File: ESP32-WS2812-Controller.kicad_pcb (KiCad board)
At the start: 2 copper layers, 60 x 50 mm, 29 parts, among them J1 USB_B_Micro, J2 Alternate_Power_Input, J3 Conn_02x03_Odd_Even, J4 Conn_01x03, Q1 Q_NPN_BEC, SW1 SW_Push, U1 AP2114HA-3.3, U2 ESP32-WROOM

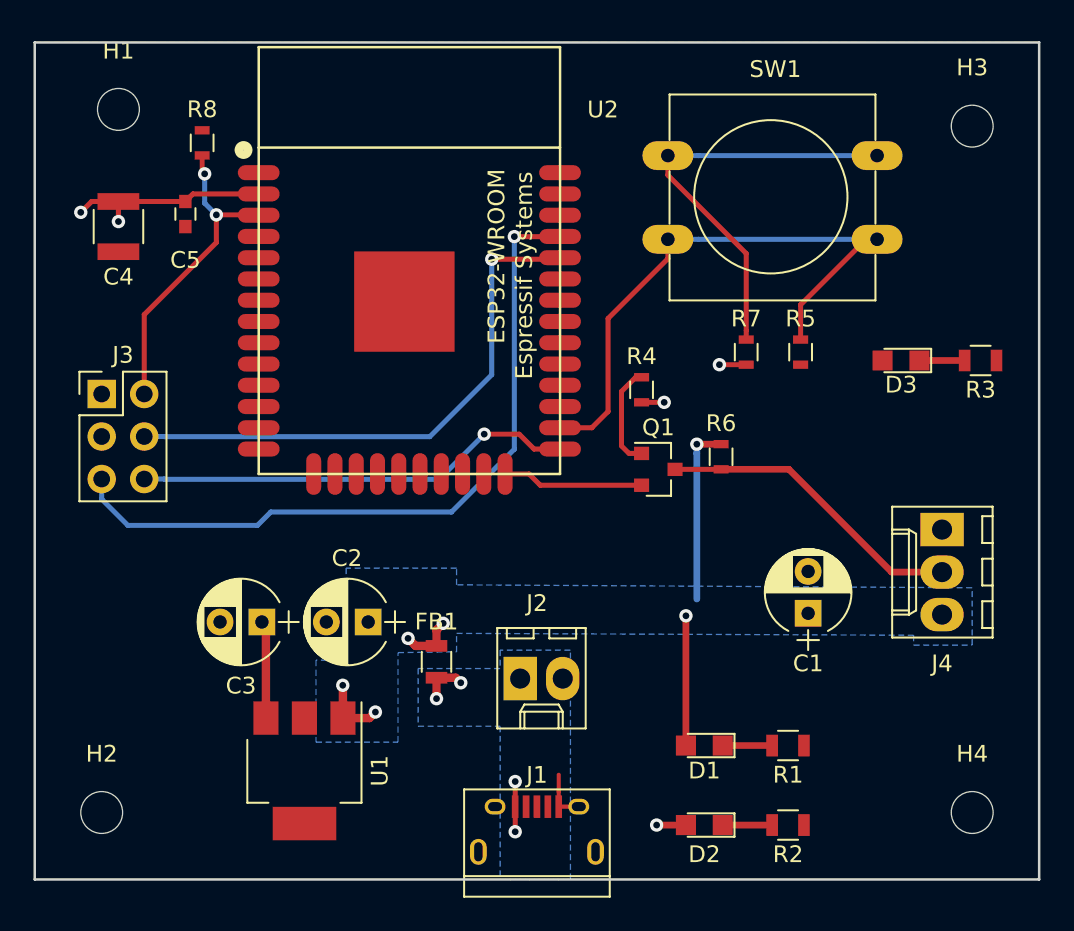
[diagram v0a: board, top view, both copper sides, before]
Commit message: Added ADC & power breakout for microphone board
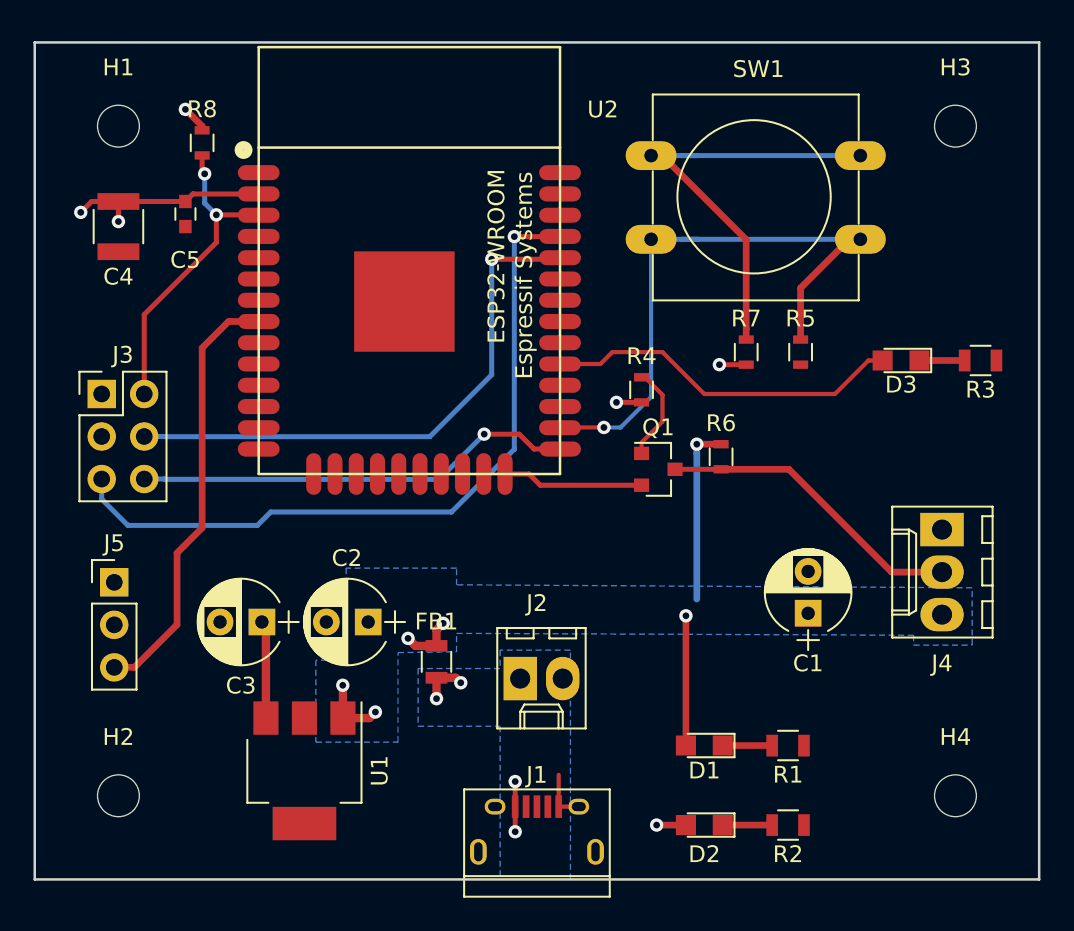
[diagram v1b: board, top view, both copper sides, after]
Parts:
- added J5: Conn_01x03, Pin_Headers:Pin_Header_Straight_1x03_Pitch2.54mm, F.Cu at (104.8, 132.2)
- moved H2 1.41 mm to (105.0, 145.0)
- moved H4 1.41 mm to (155.0, 145.0)
- moved H1 1.00 mm to (105.0, 105.0)
- moved H3 1.00 mm to (155.0, 105.0)
- moved SW1 1.00 mm to (149.3, 111.8)
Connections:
- U2 pad 8: /ESP32-WROOM/IO32 -> /Mic_Input
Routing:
- net /Mic_Input: track 0.00 -> 26.0 mm
- net /ESP32-WROOM/IO5: track 0.00 -> 21.4 mm
- net +3V3: track 22.8 -> 24.6 mm, vias 5 -> 6
- net /ESP32-WROOM/IO4: track 35.8 -> 37.5 mm, vias 0 -> 1
- net /Button_Open_Side: track 25.4 -> 26.2 mm

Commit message: Plotted gerber files and tweaked solder mask clearances.
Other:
- rule pad_to_mask_clearance: 0.051 -> 0.02
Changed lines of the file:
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@@
     (pad_size 1.524 1.524)
     (pad_drill 0.762)
-    (pad_to_mask_clearance 0.051)
+    (pad_to_mask_clearance 0.02)
     (solder_mask_min_width 0.25)
     (aux_axis_origin 0 0)
     (visible_elements FFFFFF7F)
     (pcbplotparams
-      (layerselection 0x010fc_ffffffff)
+      (layerselection 0x010f0_ffffffff)
       (usegerberextensions false)
       (usegerberattributes false)
@@
       (outputformat 1)
       (mirror false)
-      (drillshape 1)
+      (drillshape 0)
       (scaleselection 1)
-      (outputdirectory ""))
+      (outputdirectory "Gerbers/"))
   )
   (net 0 "")
@@
   (segment (start 141.1 142) (end 144.05 142) (width 0.4) (layer F.Cu) (net 4))
   (segment (start 141.1 146.75) (end 144.05 146.75) (width 0.4) (layer F.Cu) (net 5))
-  (segment (start 134.5 118.5) (end 133.79 119.21) (width 0.25) (layer F.Cu) (net 6) (status 1000000))
-  (segment (start 133.79 119.21) (end 131.38 119.21) (width 0.25) (layer F.Cu) (net 6) (status 1000000))
-  (segment (start 137.5 118.5) (end 134.5 118.5) (width 0.25) (layer F.Cu) (net 6) (status 1000000))
-  (segment (start 140 121) (end 137.5 118.5) (width 0.25) (layer F.Cu) (net 6) (status 1000000))
-  (segment (start 147.8 121) (end 140 121) (width 0.25) (layer F.Cu) (net 6) (status 1000000))
-  (segment (start 150.65 119) (end 149.8 119) (width 0.25) (layer F.Cu) (net 6) (status 1000000))
-  (segment (start 149.8 119) (end 147.8 121) (width 0.25) (layer F.Cu) (net 6) (status 1000000))
-  (segment (start 152.85 119) (end 155.55 119) (width 0.4) (layer F.Cu) (net 7) (status 1000000))
+  (segment (start 134.5 118.5) (end 133.79 119.21) (width 0.25) (layer F.Cu) (net 6))
+  (segment (start 133.79 119.21) (end 131.38 119.21) (width 0.25) (layer F.Cu) (net 6))
+  (segment (start 137.5 118.5) (end 134.5 118.5) (width 0.25) (layer F.Cu) (net 6))
+  (segment (start 140 121) (end 137.5 118.5) (width 0.25) (layer F.Cu) (net 6))
+  (segment (start 147.8 121) (end 140 121) (width 0.25) (layer F.Cu) (net 6))
+  (segment (start 150.65 119) (end 149.8 119) (width 0.25) (layer F.Cu) (net 6))
+  (segment (start 149.8 119) (end 147.8 121) (width 0.25) (layer F.Cu) (net 6))
+  (segment (start 152.85 119) (end 155.55 119) (width 0.4) (layer F.Cu) (net 7))
   (via (at 128.7 144.15) (size 0.8) (drill 0.4) (layers F.Cu B.Cu) (net 8))
   (segment (start 128.7 145.65) (end 128.7 144.15) (width 0.3) (layer F.Cu) (net 8))

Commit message: Added PCB/author information on bottom silkscreen layer and added some connector information on top silkscreen layer.
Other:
- board text added: "3.3V"
- board text added: "5V"
- board text added: "Author:"
- board text added: "Connor Driscoll"
- board text added: "ESP32 LED"
- board text added: "GND"
- board text added: "Mic Input"
- board text added: "PCB:"
- board text added: "Rev A"
- board text added: "Revision:"
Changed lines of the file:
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@@
   (general
     (thickness 1.6)
-    (drawings 4)
+    (drawings 39)
     (tracks 135)
     (zones 0)
@@
     )
   )
+  (gr_text "Rev A" (at 122.5 106.75) (layer B.SilkS)
+    (effects (font (size 1 1) (thickness 0.2)) (justify mirror))
+  )
+  (gr_text "Connor Driscoll" (at 118.75 104.5) (layer B.SilkS)
+    (effects (font (size 1 1) (thickness 0.2)) (justify mirror))
+  )
+  (gr_text "ESP32 LED" (at 120.5 102.5) (layer B.SilkS)
+    (effects (font (size 1 1) (thickness 0.2)) (justify mirror))
+  )
+  (gr_line (start 125 103.5) (end 112.5 103.5) (layer B.SilkS) (width 0.2))
+  (gr_line (start 125 105.75) (end 112.5 105.75) (layer B.SilkS) (width 0.2))
+  (gr_line (start 112.5 107.75) (end 125 107.75) (layer B.SilkS) (width 0.2))
+  (gr_line (start 112.5 101.5) (end 112.5 107.75) (layer B.SilkS) (width 0.2))
+  (gr_line (start 125 101.5) (end 112.5 101.5) (layer B.SilkS) (width 0.2))
+  (gr_line (start 132.25 103.5) (end 125 103.5) (layer B.SilkS) (width 0.2))
+  (gr_line (start 125 105.75) (end 132.25 105.75) (layer B.SilkS) (width 0.2))
+  (gr_line (start 125 101.5) (end 132.25 101.5) (layer B.SilkS) (width 0.2))
+  (gr_line (start 125 107.75) (end 125 101.5) (layer B.SilkS) (width 0.2))
+  (gr_line (start 132.25 107.75) (end 125 107.75) (layer B.SilkS) (width 0.2))
+  (gr_line (start 132.25 101.5) (end 132.25 107.75) (layer B.SilkS) (width 0.2))
+  (gr_text Revision: (at 128.5 106.75) (layer B.SilkS)
+    (effects (font (size 1 1) (thickness 0.2)) (justify mirror))
+  )
+  (gr_text Author: (at 129.25 104.5) (layer B.SilkS)
+    (effects (font (size 1 1) (thickness 0.2)) (justify mirror))
+  )
+  (gr_text PCB: (at 130 102.5) (layer B.SilkS)
+    (effects (font (size 1 1) (thickness 0.2)) (justify mirror))
+  )
+  (gr_text 5V (at 129 131) (layer F.SilkS)
+    (effects (font (size 1 1) (thickness 0.2)))
+  )
+  (gr_line (start 129 136.5) (end 129 131.75) (layer F.SilkS) (width 0.2))
+  (gr_line (start 134 139) (end 135.5 139) (layer F.SilkS) (width 0.2))
+  (gr_line (start 134.5 140) (end 135 140) (layer F.SilkS) (width 0.2))
+  (gr_line (start 134.25 139.5) (end 135.25 139.5) (layer F.SilkS) (width 0.2))
+  (gr_line (start 134.75 138) (end 134.75 139) (layer F.SilkS) (width 0.2))
+  (gr_line (start 132.75 138) (end 134.75 138) (layer F.SilkS) (width 0.2))
+  (gr_line (start 154 124.5) (end 154.5 124.5) (layer F.SilkS) (width 0.2))
+  (gr_line (start 153.75 125) (end 154.75 125) (layer F.SilkS) (width 0.2))
+  (gr_line (start 153.5 125.5) (end 155 125.5) (layer F.SilkS) (width 0.2))
+  (gr_line (start 154.25 127.75) (end 154.25 125.5) (layer F.SilkS) (width 0.2))
+  (gr_line (start 103.75 116.25) (end 104.25 116.25) (layer F.SilkS) (width 0.2))
+  (gr_line (start 103.5 116.75) (end 104.5 116.75) (layer F.SilkS) (width 0.2))
+  (gr_line (start 103.25 117.25) (end 104.75 117.25) (layer F.SilkS) (width 0.2))
+  (gr_line (start 104 120) (end 104 117.25) (layer F.SilkS) (width 0.2))
+  (gr_text "Mic\nInput" (at 108.25 137.75) (layer F.SilkS)
+    (effects (font (size 1 1) (thickness 0.2)))
+  )
+  (gr_text GND (at 108 134.75) (layer F.SilkS)
+    (effects (font (size 1 1) (thickness 0.2)))
+  )
+  (gr_text 3.3V (at 108.25 132) (layer F.SilkS)
+    (effects (font (size 1 1) (thickness 0.2)))
+  )
   (gr_line (start 100 100) (end 160 100) (layer Edge.Cuts) (width 0.15))
